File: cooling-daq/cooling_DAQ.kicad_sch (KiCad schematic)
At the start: 56 parts, among them J1 Conn_02x10_Odd_Even, J1 USB_C_Receptacle_USB2.0_16P, J2 Conn_01x03_Pin, J3 Conn_01x02_Pin, J4 Conn_01x02_Pin, Q1 2N7002, Q2 2N7002, Q3 Si2301CDS, SW1 SW_SPST, U1 STM32F103C8Tx, U2 AP2204K-ADJ, U3 AP2204K-ADJ, U6 SN65HVD256D, Y1 8M, Y2 32.768k

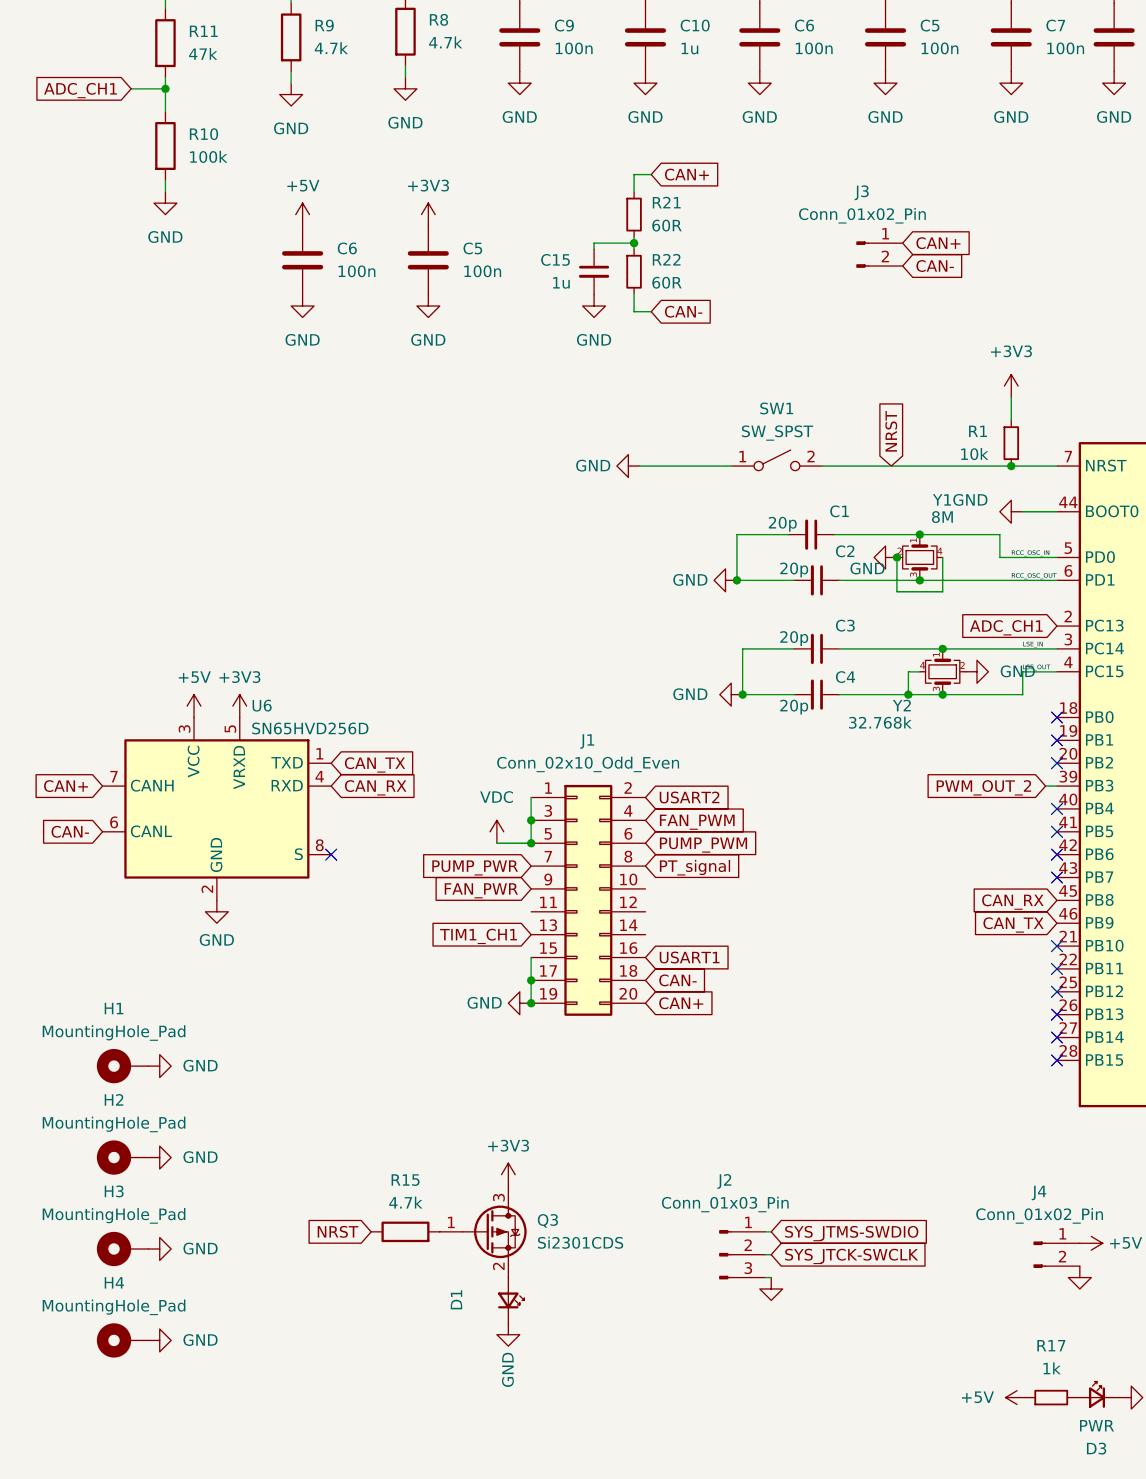
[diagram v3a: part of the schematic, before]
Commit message: fix: SWDIO LED & CAN jumper
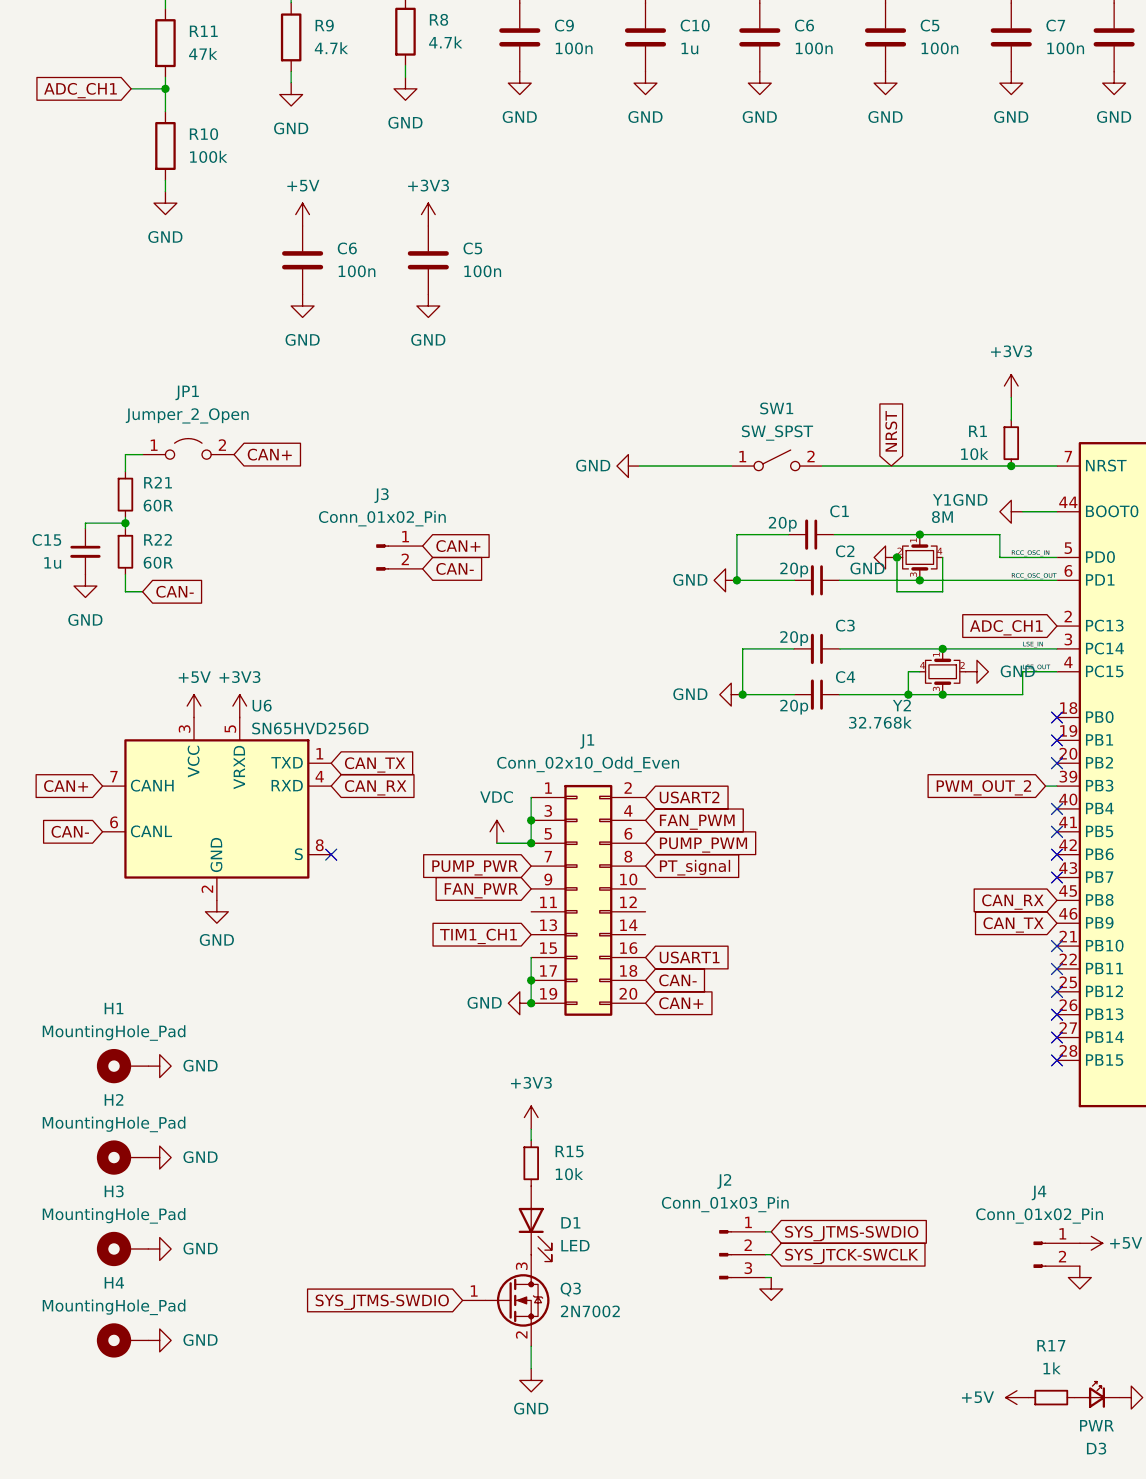
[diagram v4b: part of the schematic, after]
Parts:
- removed D1: ~, LED_SMD:LED_0805_2012Metric, symbol Device:LED_Small
- removed Q3: Si2301CDS, Package_TO_SOT_SMD:SOT-23, symbol Transistor_FET:Si2319CDS
- removed R15: 4.7k, Resistor_SMD:R_0603_1608Metric, symbol Device:R
- added D1: LED, LED_SMD:LED_0805_2012Metric, symbol Device:LED
- added JP1: Jumper_2_Open, Connector_PinHeader_2.54mm:PinHeader_1x02_P2.54mm_Vertical, symbol Jumper:Jumper_2_Open
- added Q3: 2N7002, Package_TO_SOT_SMD:SOT-23, symbol Transistor_FET:2N7002
- added R15: 10k, Resistor_SMD:R_0603_1608Metric, symbol Device:R_Small
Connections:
- net +3V3: now also R15.1
- net CAN+: now also JP1.2 (B); no longer R21.1
- net GND: now also Q3.2 (S)
- net SYS_JTMS-SWDIO: now also Q3.1 (G)
- new net: D1.2 (A), R15.2
- new net: D1.1 (K), Q3.3 (D)
- new net: JP1.1 (A), R21.1
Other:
- moved on the sheet: C15, J3, R21, R22

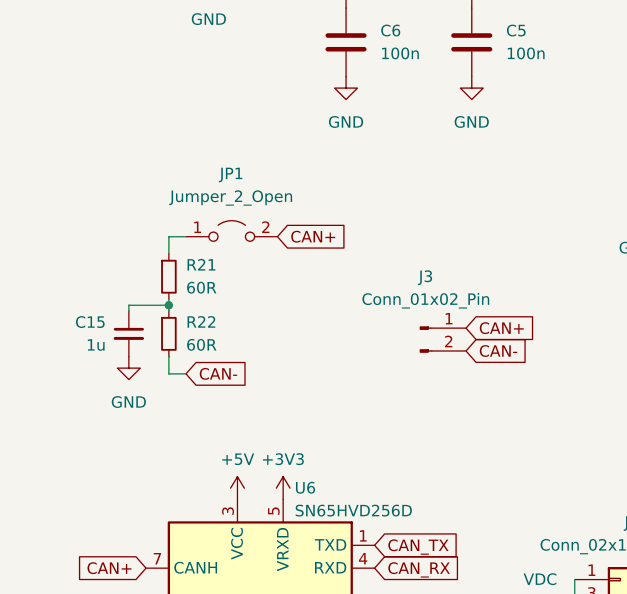
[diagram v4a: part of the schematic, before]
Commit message: feat: add ESD in CAN
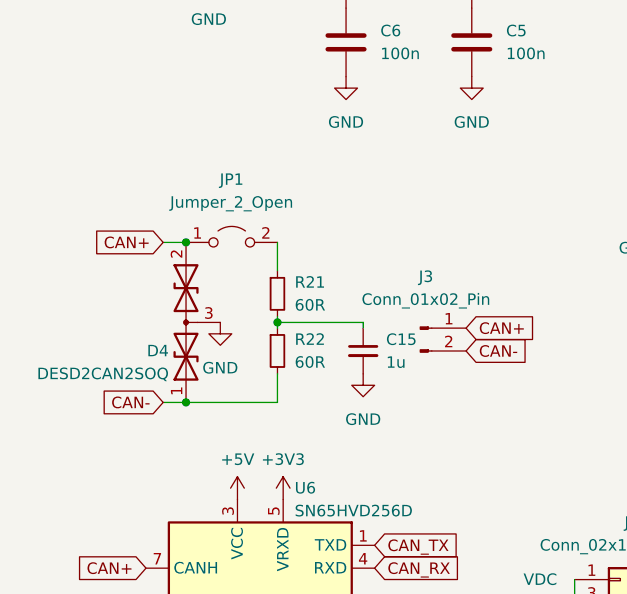
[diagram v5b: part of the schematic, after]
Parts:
- added D4: DESD2CAN2SOQ, Package_TO_SOT_SMD:TSOT-23, symbol Device:D_TVS_Dual_AAC
- JP1: footprint Connector_PinHeader_2.54mm:PinHeader_1x02_P2.54mm_Vertical -> TestPoint:TestPoint_2Pads_Pitch2.54mm_Drill0.8mm
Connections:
- net CAN+: now also JP1.1 (A), D4.2 (A2); no longer JP1.2 (B)
- net CAN-: now also D4.1 (A1)
- net GND: now also D4.3 (common)
- net at R21.1: now also JP1.2 (B); no longer JP1.1 (A)
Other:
- moved on the sheet: C15, R21, R22

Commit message: feat: redesign
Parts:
- removed C10, C11: 1u, Resistor_SMD:R_0603_1608Metric, symbol Device:C
- removed C12: 10u, Resistor_SMD:R_0805_2012Metric, symbol Device:C
- removed C3, C4: 20p, Capacitor_SMD:C_0603_1608Metric, symbol Device:C_Small
- removed C5: 100n, Resistor_SMD:R_0603_1608Metric, symbol Device:C
- removed D1: LED, LED_SMD:LED_0805_2012Metric, symbol Device:LED
- removed D2: BAT46W-7-F, Diode_SMD:D_SOD-123, symbol Diode:1N4148W
- removed J1: USB_C_Receptacle_USB2.0_16P, Connector_USB:USB_C_Receptacle_HRO_TYPE-C-31-M-12, symbol Connector:USB_C_Receptacle_USB2.0_16P
- removed J1: Conn_02x10_Odd_Even, Connector_PinHeader_2.54mm:PinHeader_2x10_P2.54mm_Vertical, symbol Connector_Generic:Conn_02x10_Odd_Even
- removed J3, J4: Conn_01x02_Pin, Connector_PinHeader_2.54mm:PinHeader_1x02_P2.54mm_Vertical, symbol Connector:Conn_01x02_Pin
- removed Q3: 2N7002, Package_TO_SOT_SMD:SOT-23, symbol Transistor_FET:2N7002
- removed R10, R2: 100k, Resistor_SMD:R_0603_1608Metric, symbol Device:R
- removed R11: 47k, Resistor_SMD:R_0603_1608Metric, symbol Device:R
- removed R15, R16: 10k, Resistor_SMD:R_0603_1608Metric, symbol Device:R_Small
- removed R3: 301k, Resistor_SMD:R_0603_1608Metric, symbol Device:R
- removed R6, R7: 5k1, Resistor_SMD:R_0603_1608Metric, symbol Device:R_Small
- removed R8, R9: 4.7k, Resistor_SMD:R_0603_1608Metric, symbol Device:R
- removed SW1: SW_SPST, Button_Switch_SMD:SW_SPST_FSMSM, symbol Switch:SW_SPST
- removed U2: AP2204K-ADJ, Package_TO_SOT_SMD:SOT-23-5, symbol Regulator_Linear:AP2204K-ADJ
- removed Y2: 32.768k, Crystal:Crystal_SMD_SeikoEpson_FA238-4Pin_3.2x2.5mm, symbol Device:Crystal_GND24_Small
- added J1: Conn_PWR, Connector_JST:JST_XH_B2B-XH-A_1x02_P2.50mm_Vertical, symbol Connector_Generic:Conn_01x02
- added J4: Conn_01x04, Connector_JST:JST_XH_B4B-XH-A_1x04_P2.50mm_Vertical, symbol Connector_Generic:Conn_01x04
- added J5: Conn_01x02, Connector_JST:JST_XH_B2B-XH-A_1x02_P2.50mm_Vertical, symbol Connector_Generic:Conn_01x02
- added R1: 10k, Resistor_SMD:R_0603_1608Metric, symbol Device:R_Small
- added U2: TME-2405S, Converter_DCDC:Converter_DCDC_TRACO_TME_24xxS_Single_THT, symbol Converter_DCDC:TME-2405S
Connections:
- net FAN_PWR is gone; now on net +5V: R14.2
- net +5V: now also J4.1 (Pin_1), R1.2, U2.4 (+Vout)
- net CAN+: now also J5.2 (Pin_2)
- net CAN-: now also J5.1 (Pin_1)
- net FAN_PWM: now also J4.2 (Pin_2)
- net GND: now also U6.8 (S), J1.1 (Pin_1), J4.4 (Pin_4), U2.1 (-Vin), U2.3 (-Vout)
- net PWM_OUT: now also Q2.1 (G); no longer Q1.1 (G)
- net PWM_OUT_2: now also Q1.1 (G); no longer Q2.1 (G)
- net ADC_CH1: no longer names the net of U1.2 (PC13)
- net LSE_IN: no longer names the net of U1.3 (PC14)
- net LSE_OUT: no longer names the net of U1.4 (PC15)
- net NRST: no longer names the net of R1.2, U1.7 (NRST)
- net PUMP_PWM renamed FAN_PWM2
- net FAN_PWM2: now also J4.3 (Pin_3), R1.1
- new net: J1.2 (Pin_2), U2.2 (+Vin)
- no-connect marks 24 -> 21
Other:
- moved on the sheet: C1, C13, C14, C15, C2, C5, C6, C7, C8, C9, D3, D4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
